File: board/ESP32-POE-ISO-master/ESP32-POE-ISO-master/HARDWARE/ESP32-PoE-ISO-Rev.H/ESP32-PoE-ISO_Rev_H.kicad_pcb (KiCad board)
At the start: 4 copper layers, 28 x 93 mm, 137 parts, among them Q1 Q12MHz/20pF/10ppm/4P/3.2x2.5mm, Q2 BC817-40(SOT23), Q3 BC817-40(SOT23), T1 LMUN2211LT1G(SOT-23), U1 CH340T(SSOP20W), U2 TPS2375PW(TSSOP-8), U3 BL4054B-42TPRN(SOT23-5), U4 LAN8710A-EZC(QFN32), U5 TX4138(ESOIC-8), U7 SY8089AAAC(SOT23-5), U9 ESP32-WROOM-32D-4MB

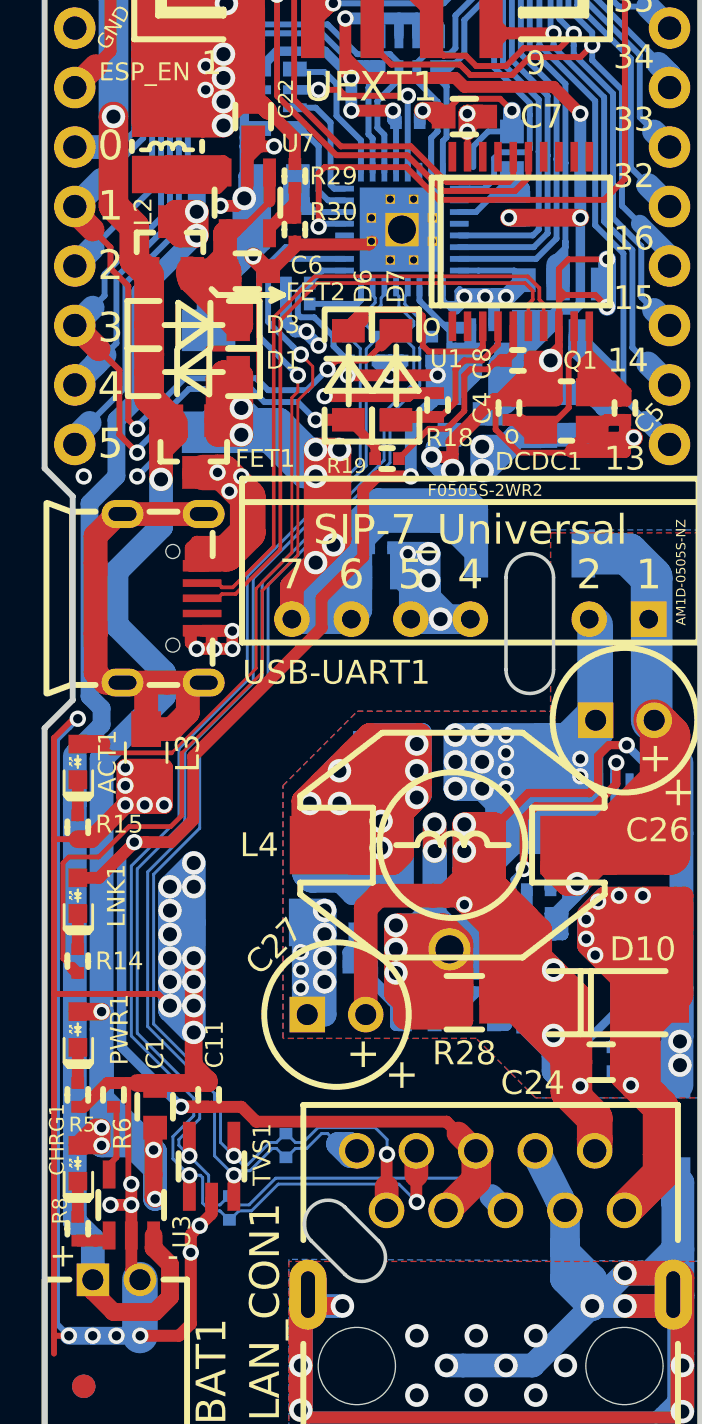
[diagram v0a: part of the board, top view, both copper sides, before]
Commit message: commit début placage
début du placage sans les bouttons
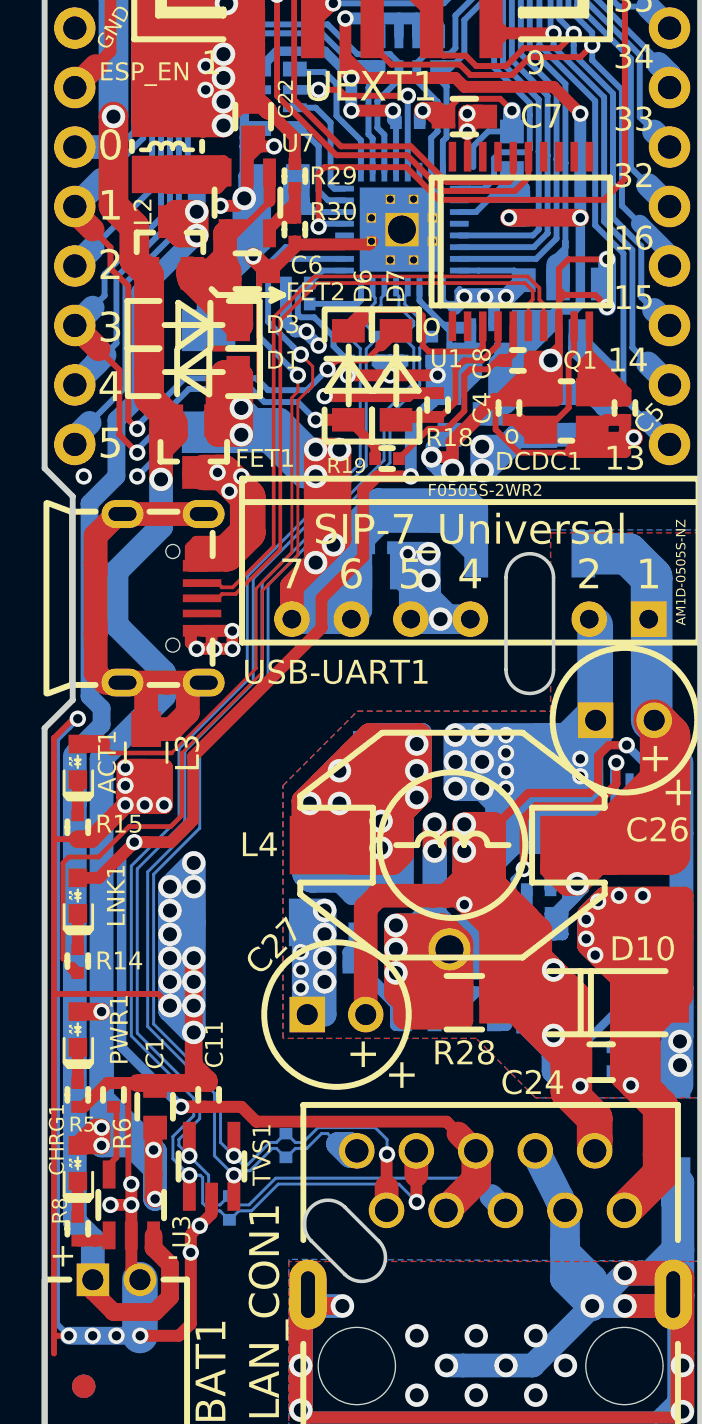
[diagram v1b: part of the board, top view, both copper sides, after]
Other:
- net class Default removed
- net class Diff_Z=100 removed
- net class Diff_Z=90 removed
